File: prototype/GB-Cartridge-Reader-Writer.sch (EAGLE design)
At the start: 37 parts, among them IC1 74HC595N, IC2 74HC595N

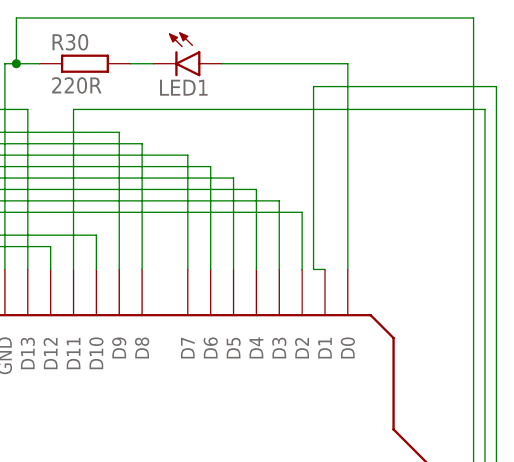
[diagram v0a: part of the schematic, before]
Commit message: moved some components - no functionial changes
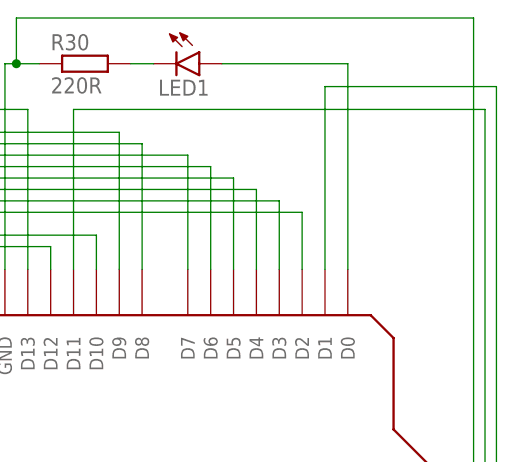
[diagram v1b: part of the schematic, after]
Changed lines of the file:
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@@
 <?xml version="1.0" encoding="utf-8"?>
 <!DOCTYPE eagle SYSTEM "eagle.dtd">
-<eagle version="9.3.0">
+<eagle version="9.4.0">
 <drawing>
 <settings>
@@
 </segment>
 </net>
-<net name="N$27" class="0">
-<segment>
-<wire x1="-43.18" y1="-83.82" x2="96.52" y2="-83.82" width="0.1524" layer="91"/>
-<pinref part="R26" gate="G$1" pin="2"/>
-<wire x1="96.52" y1="-83.82" x2="96.52" y2="88.9" width="0.1524" layer="91"/>
-<wire x1="96.52" y1="88.9" x2="76.2" y2="88.9" width="0.1524" layer="91"/>
-<pinref part="U$1" gate="G$1" pin="D1"/>
-<wire x1="76.2" y1="88.9" x2="76.2" y2="68.58" width="0.1524" layer="91"/>
-<wire x1="76.2" y1="68.58" x2="77.47" y2="68.58" width="0.1524" layer="91"/>
-</segment>
-</net>
 <net name="N$50" class="0">
 <segment>
@@
 </segment>
 </net>
+<net name="N$46" class="0">
+<segment>
+<pinref part="U$1" gate="G$1" pin="D1"/>
+<wire x1="-43.18" y1="-83.82" x2="96.52" y2="-83.82" width="0.1524" layer="91"/>
+<pinref part="R26" gate="G$1" pin="2"/>
+<wire x1="96.52" y1="-83.82" x2="96.52" y2="88.9" width="0.1524" layer="91"/>
+<wire x1="96.52" y1="88.9" x2="77.47" y2="88.9" width="0.1524" layer="91"/>
+<wire x1="77.47" y1="68.58" x2="77.47" y2="88.9" width="0.1524" layer="91"/>
+</segment>
+</net>

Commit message: made traces wider; wired wire bridges on bottom layer to get the vias for drilling; more space between traces;
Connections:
- net N$51: now also S1.S1
- net N$65: now also S1.P1
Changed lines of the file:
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@@
 <?xml version="1.0" encoding="utf-8"?>
 <!DOCTYPE eagle SYSTEM "eagle.dtd">
-<eagle version="9.4.0">
+<eagle version="9.3.0">
 <drawing>
 <settings>
@@
 <wire x1="58.42" y1="7.62" x2="57.15" y2="7.62" width="0.1524" layer="91"/>
 <junction x="57.15" y="7.62"/>
+<pinref part="S1" gate="1" pin="S1"/>
+<wire x1="63.5" y1="-5.08" x2="63.5" y2="-2.54" width="0.1524" layer="91"/>
+<junction x="63.5" y="-5.08"/>
 </segment>
 </net>
@@
 <pinref part="U$1" gate="G$1" pin="A0"/>
 <wire x1="69.85" y1="5.08" x2="69.85" y2="7.62" width="0.1524" layer="91"/>
-</segment>
-</net>
+<pinref part="S1" gate="1" pin="P1"/>
+<wire x1="73.66" y1="-5.08" x2="73.66" y2="-2.54" width="0.1524" layer="91"/>
+<junction x="73.66" y="-5.08"/>
+</segment>
+</net>

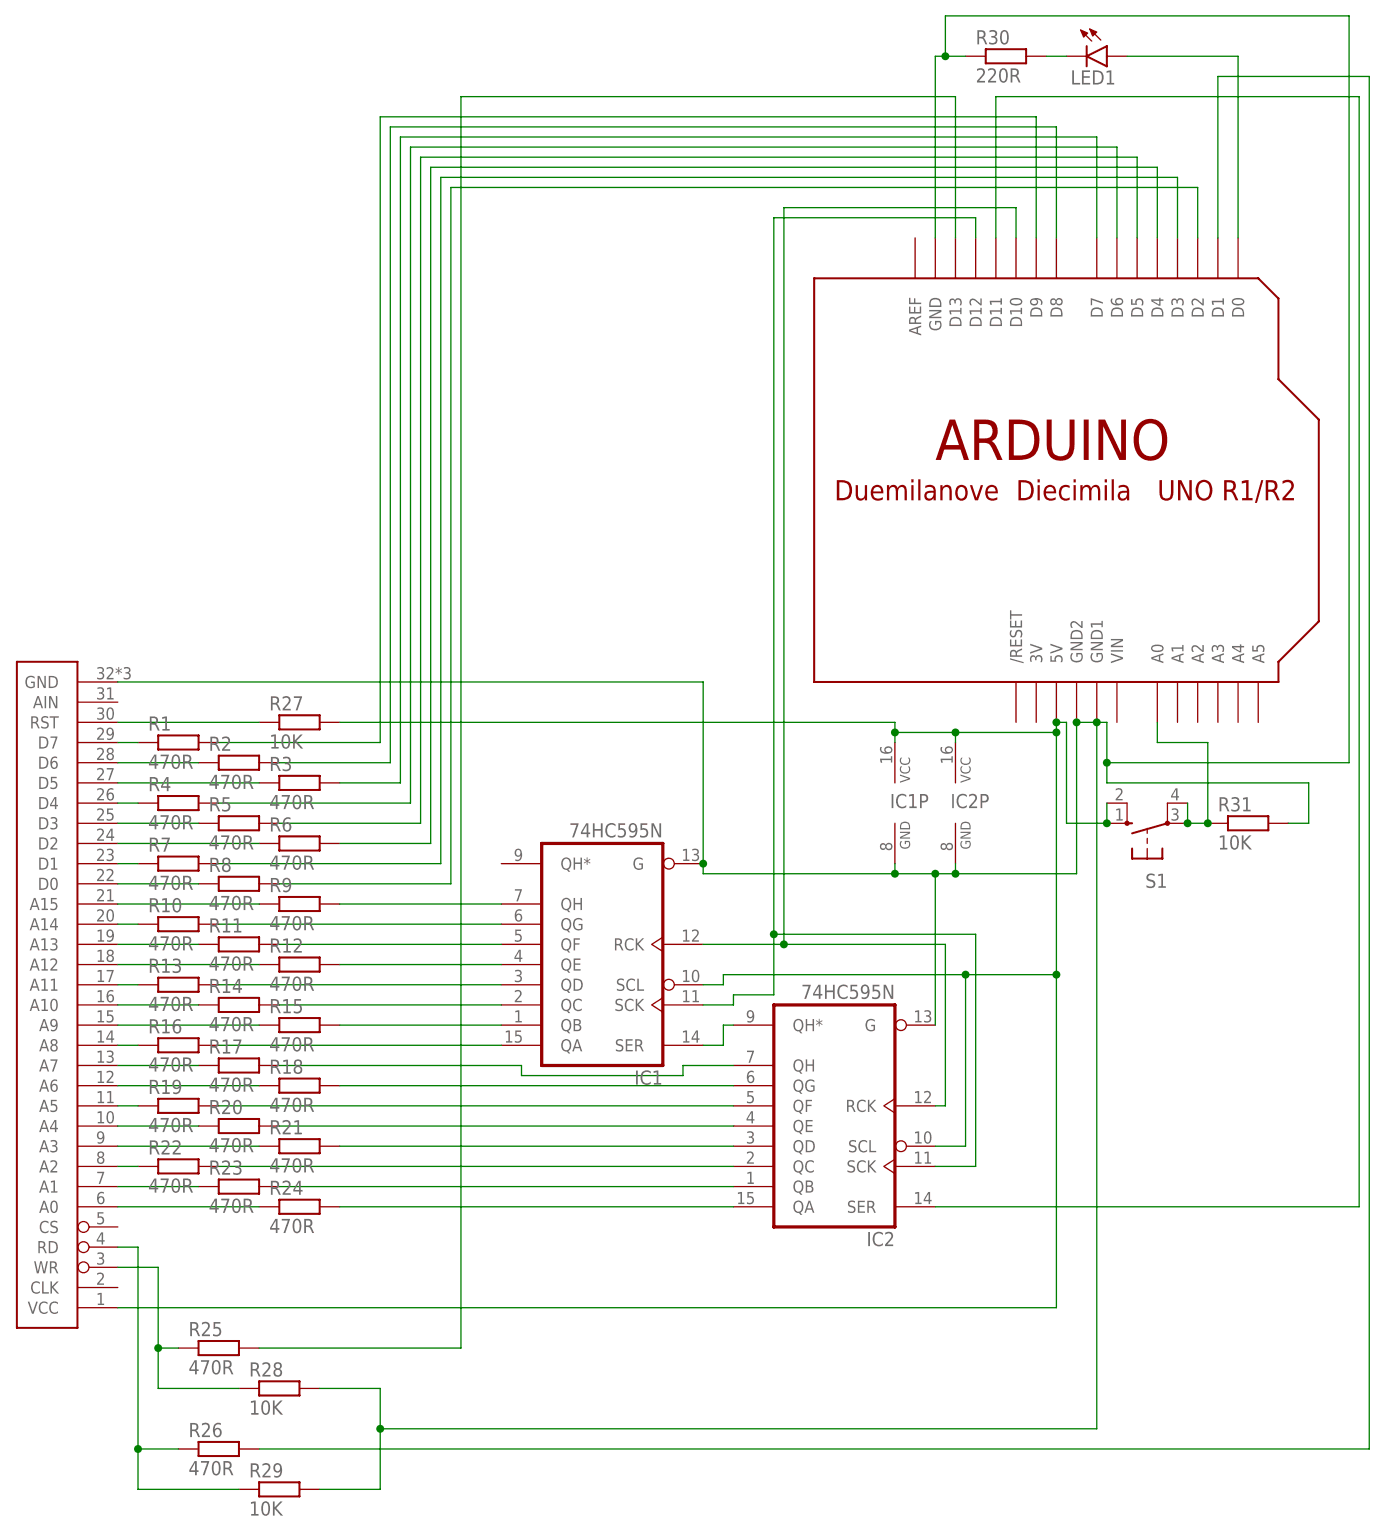
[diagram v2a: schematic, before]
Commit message: license, layout improvements, png, submodules, readme
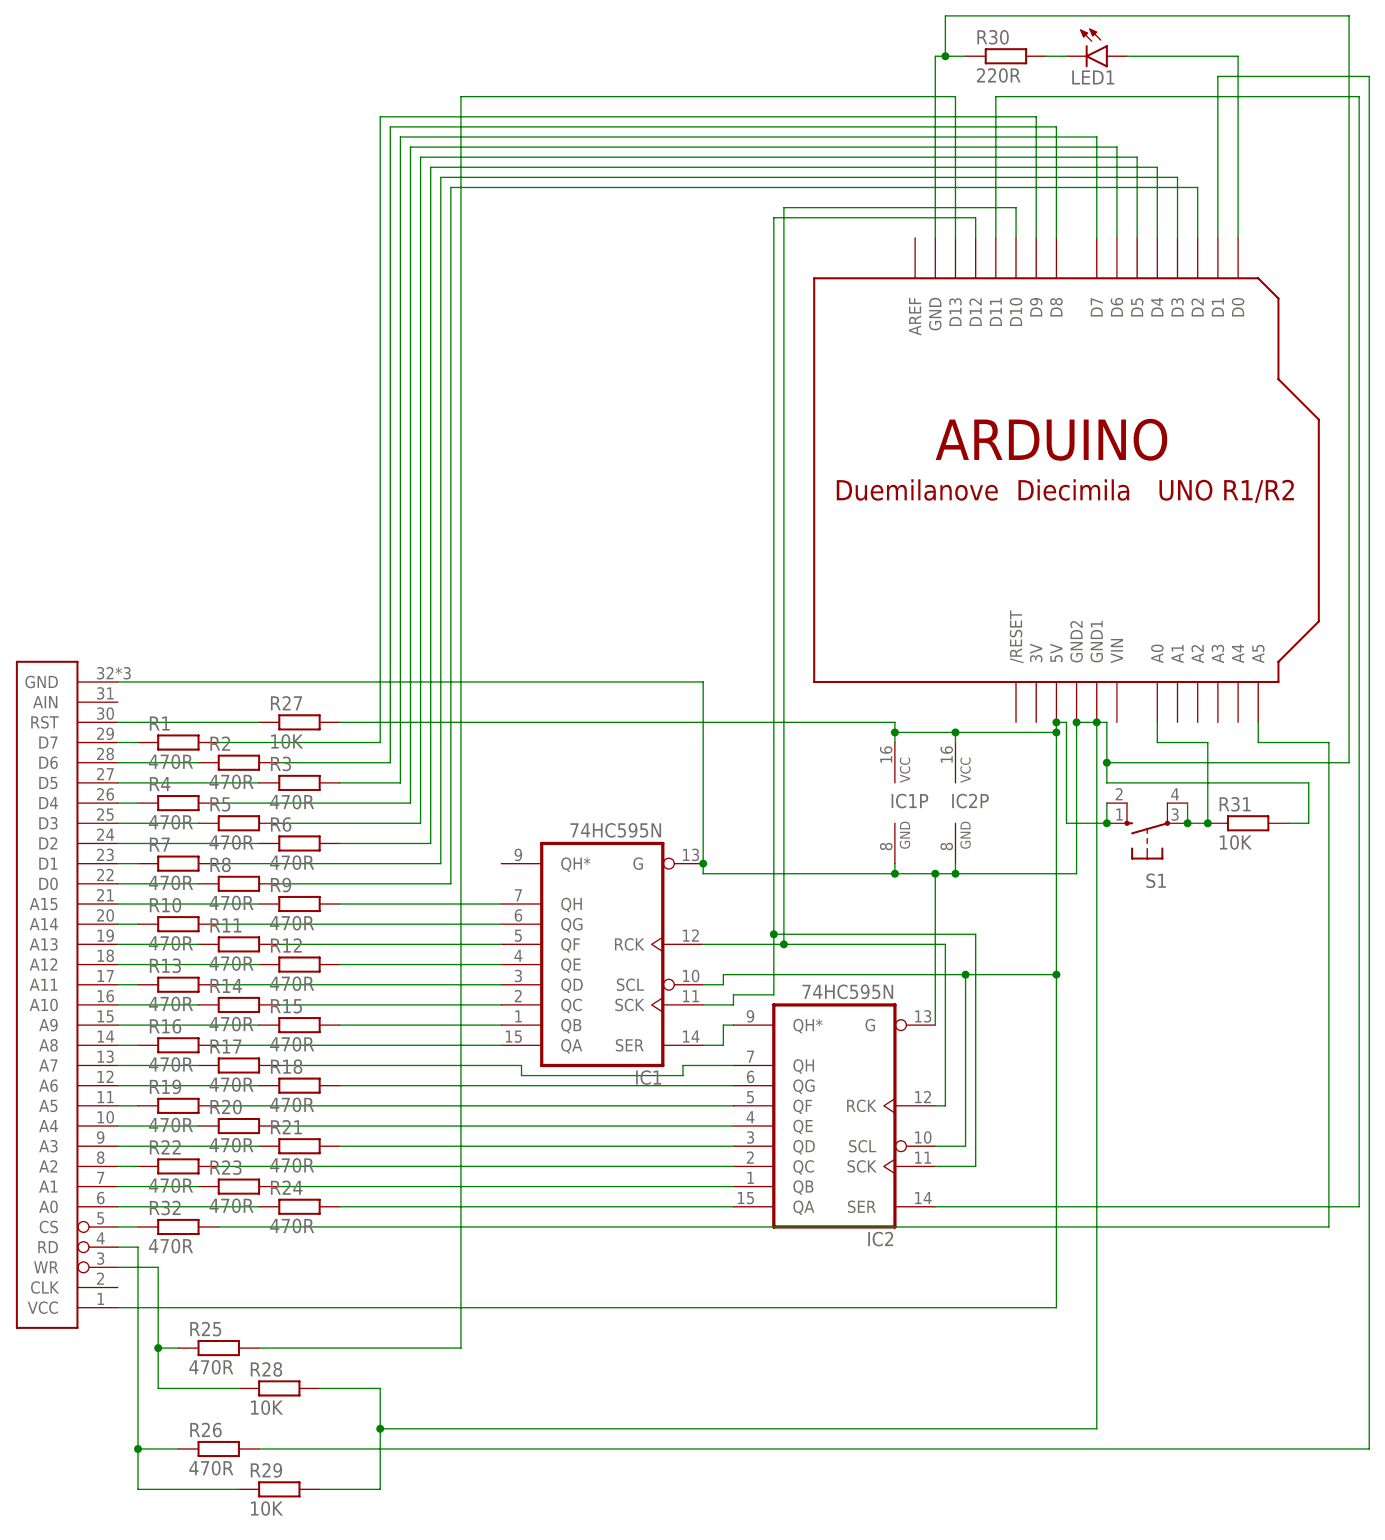
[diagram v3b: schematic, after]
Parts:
- added R32: 470R, rcl:R-EU_0207/10
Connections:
- new net N$27: R32.1, U$2.CS
- new net N$64: R32.2, U$1.A5
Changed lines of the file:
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@@
 <?xml version="1.0" encoding="utf-8"?>
 <!DOCTYPE eagle SYSTEM "eagle.dtd">
-<eagle version="9.3.0">
+<eagle version="9.5.2">
 <drawing>
 <settings>
@@
 <part name="R30" library="rcl" library_urn="urn:adsk.eagle:library:334" deviceset="R-EU_" device="0207/10" package3d_urn="urn:adsk.eagle:package:23491/1" value="220R"/>
 <part name="R31" library="rcl" library_urn="urn:adsk.eagle:library:334" deviceset="R-EU_" device="0207/10" package3d_urn="urn:adsk.eagle:package:23491/1" value="10K"/>
+<part name="R32" library="rcl" library_urn="urn:adsk.eagle:library:334" deviceset="R-EU_" device="0207/10" package3d_urn="urn:adsk.eagle:package:23491/1" value="470R"/>
 </parts>
 <sheets>
@@
 <attribute name="NAME" x="77.47" y="-3.5814" size="1.778" layer="95"/>
 <attribute name="VALUE" x="77.47" y="-8.382" size="1.778" layer="96"/>
+</instance>
+<instance part="R32" gate="G$1" x="-53.34" y="-55.88" smashed="yes">
+<attribute name="NAME" x="-57.15" y="-54.3814" size="1.778" layer="95"/>
+<attribute name="VALUE" x="-57.15" y="-59.182" size="1.778" layer="96"/>
 </instance>
 </instances>
@@
 </segment>
 </net>
+<net name="N$27" class="0">
+<segment>
+<pinref part="U$2" gate="G$1" pin="CS"/>
+<pinref part="R32" gate="G$1" pin="1"/>
+<wire x1="-60.96" y1="-55.88" x2="-58.42" y2="-55.88" width="0.1524" layer="91"/>
+</segment>
+</net>
+<net name="N$64" class="0">
+<segment>
+<pinref part="R32" gate="G$1" pin="2"/>
+<wire x1="91.44" y1="5.08" x2="91.44" y2="-55.88" width="0.1524" layer="91"/>
+<wire x1="91.44" y1="-55.88" x2="-48.26" y2="-55.88" width="0.1524" layer="91"/>
+<pinref part="U$1" gate="G$1" pin="A5"/>
+<wire x1="82.55" y1="7.62" x2="82.55" y2="5.08" width="0.1524" layer="91"/>
+<wire x1="82.55" y1="5.08" x2="91.44" y2="5.08" width="0.1524" layer="91"/>
+</segment>
+</net>
